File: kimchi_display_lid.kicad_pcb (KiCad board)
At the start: 4 copper layers, 123 x 91 mm, 44 parts, among them J1 DF40HC(3.5)-60DS, J2 DF40HC(3.5)-60DS, J3 H19C-6S-0.5SH, J4 FH19C-40S-0.5SH(10), J5 USB_A, U1 24C32, U2 AP3019AKTR-G1, U3 TXS0108EPW, U4 LSM6DSRTR, U5 TPD3S014

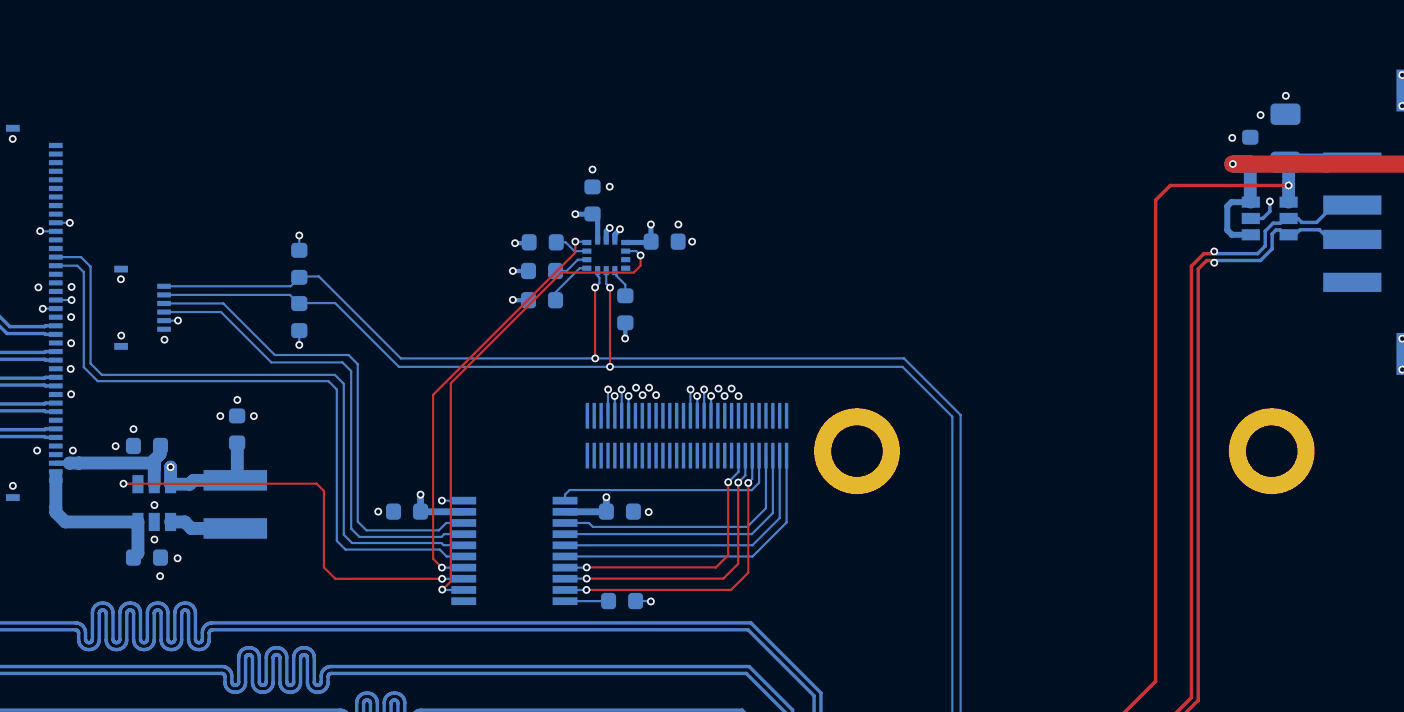
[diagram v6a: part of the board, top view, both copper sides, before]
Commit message: Add a small board to connect touchscreen
When the cables wrap around the PCB the distance between
the 40pin and 6pin connectors is too close.

The "hoverboard" floats over the 40pin connector to
air jordan the 6pin down to the main board via a stacked
connector pair.

Signed-off-by: Michael Welling <mwelling@ieee.org>
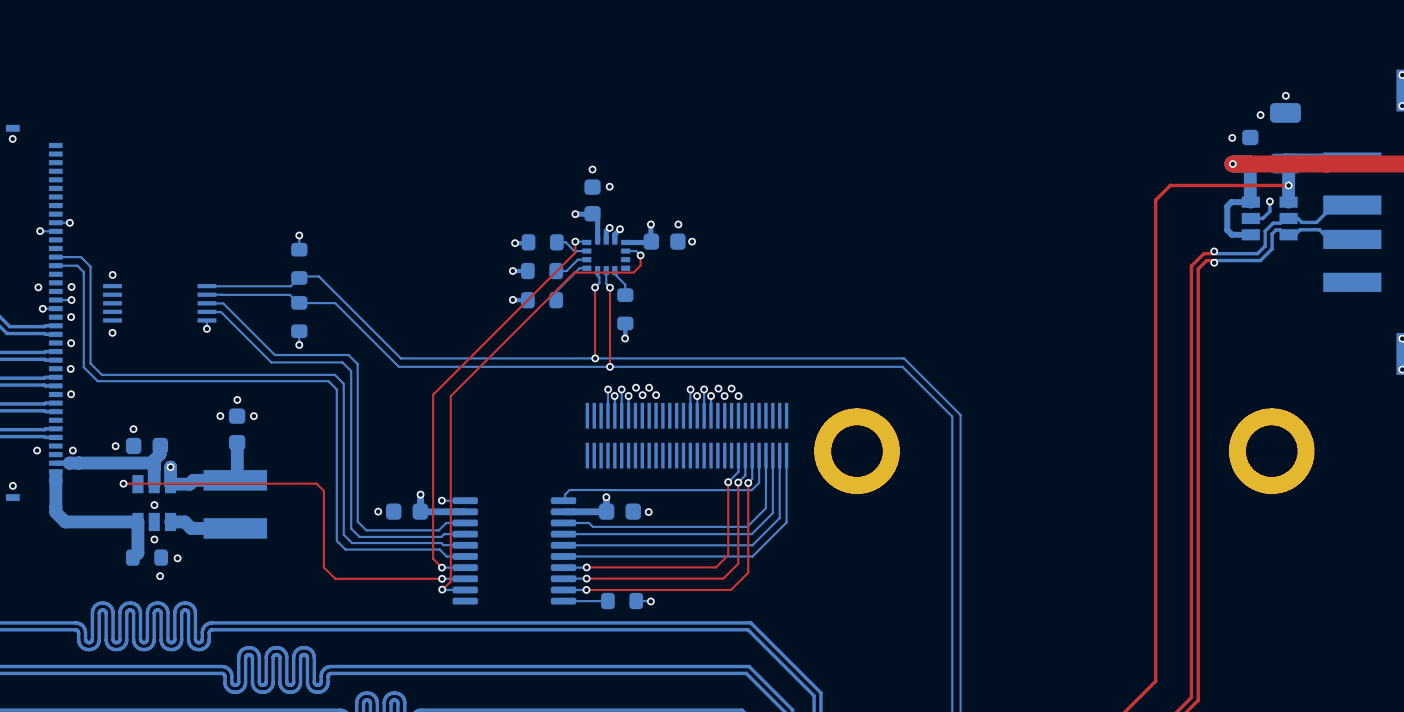
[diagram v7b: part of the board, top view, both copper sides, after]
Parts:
- added LOGO3: Logo_Open_Hardware_Small, kimchi_ulid:hoverboard-3d-model, B.Cu at (116.2, 107.2)
- J3: value H19C-6S-0.5SH -> Conn_02x05_Odd_Even; footprint kimchi_ulid:HRS_FH19C-6S-0.5SH_1x06-1MP_P0.50mm -> kimchi_ulid:HIROSE_DF23C-10DS-0.5V(51)
- moved J3 1.03 mm to (118.0, 107.2), turned to 270 degrees
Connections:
- J3 pad 1: GND -> I2C3_SDA
- J3 pad 2: VDD_3V3 -> GND
- J3 pad 3: /TS_INT -> I2C3_SCL
- J3 pad 4: /TS_RESET -> GND
- J3 pad 5: I2C3_SCL -> /TS_RESET
- J3 pad 6: I2C3_SDA -> GND
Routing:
- net /TS_RESET: track 28.5 -> 26.0 mm
- net /TS_INT: track 28.3 -> 25.8 mm
- net I2C3_SDA: track 102.6 -> 100.1 mm
- net I2C3_SCL: track 100.1 -> 97.6 mm
- net GND: vias 58 -> 57

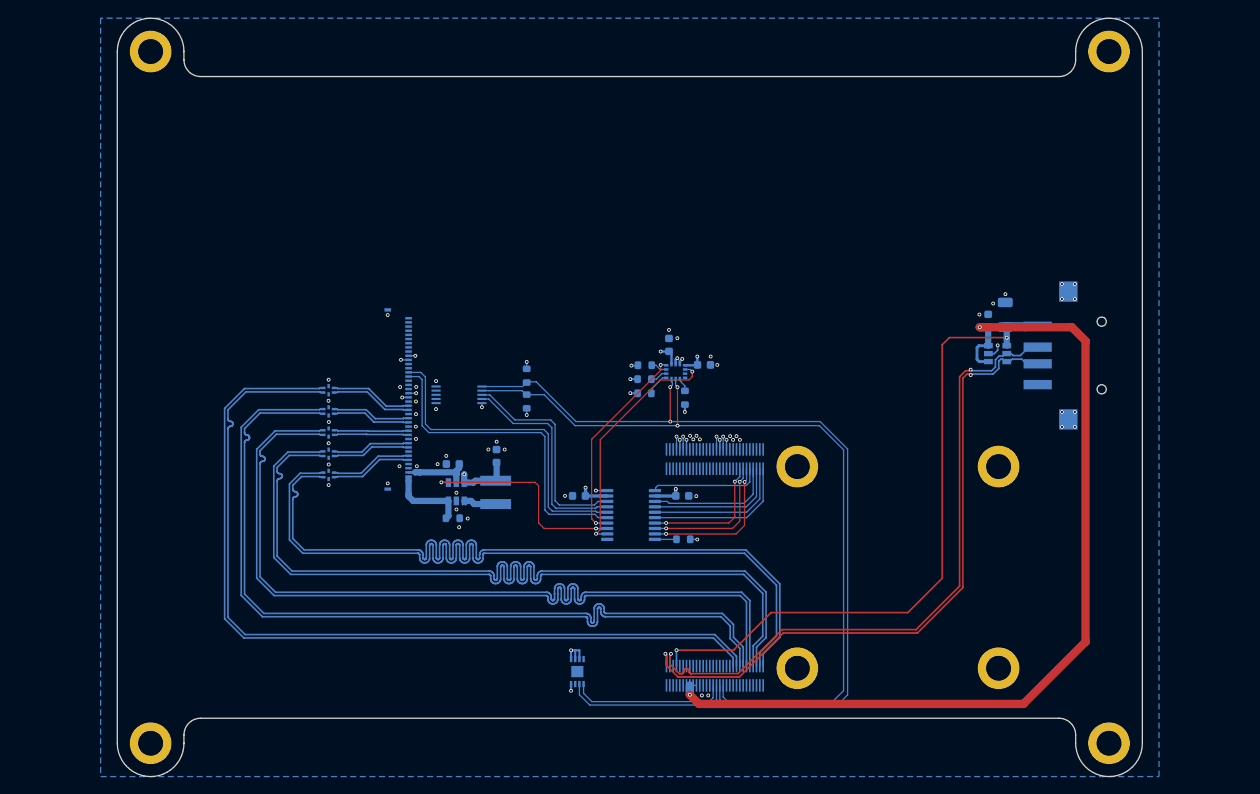
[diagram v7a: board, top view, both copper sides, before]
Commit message: Totally messed up the connections to the hoverboard
Great scott!!

Only caught this after placing an order at OSHpark.
Swiftly cancelled for this fix.

Signed-off-by: Michael Welling <mwelling@ieee.org>
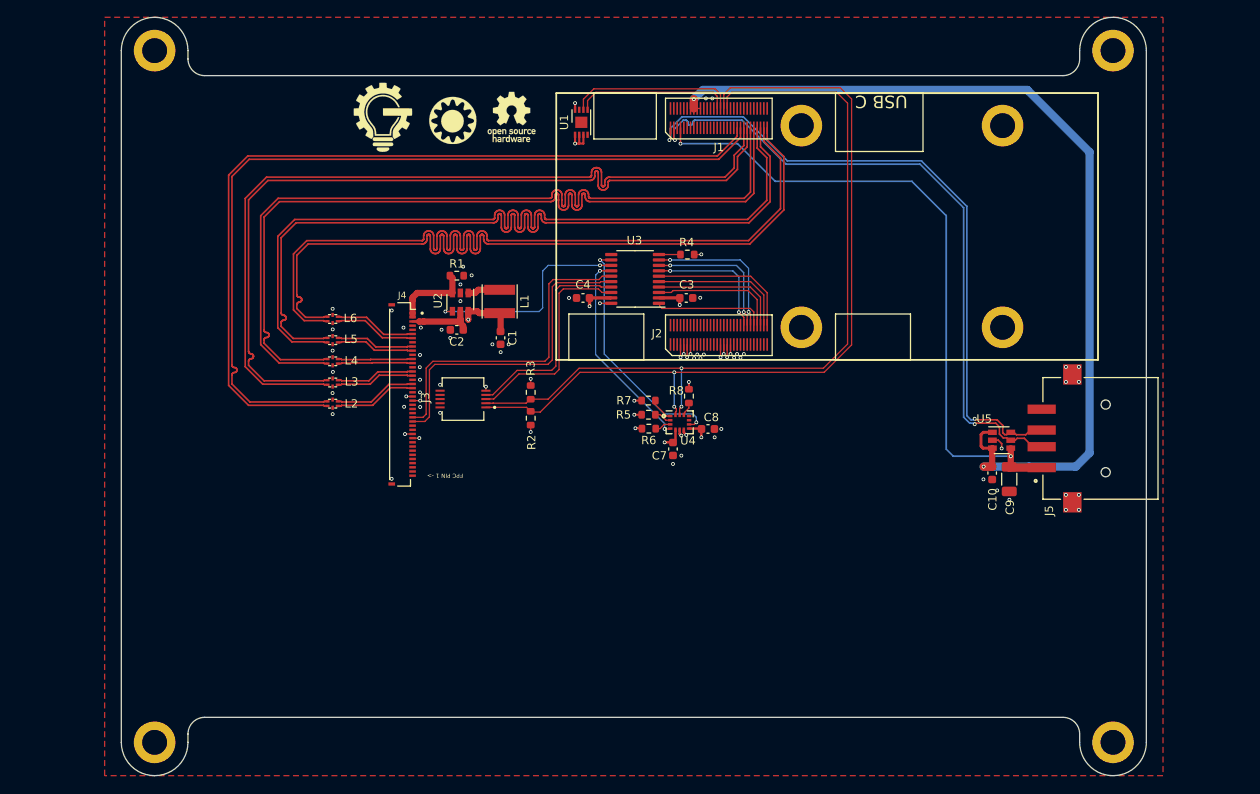
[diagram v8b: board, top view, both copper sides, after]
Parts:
- C1, C10, C2, C3, C4, C7, C8, C9, J1, J2, J3, J4, J5, L1, L2, L3, L4, L5, L6, L7, L8, LOGO1, LOGO2, LOGO3, R1, R2, R3, R4, R5, R6, R7, R8, U1, U2, U3, U4, U5: moved to F.Cu
- H1, H2, H3, H4, H5, H6, H7, H8: moved to B.Cu
- moved H5 83.1 mm to (81.5, 65.9)
- moved H8 83.1 mm to (196.5, 65.9)
- moved H6 82.9 mm to (81.5, 148.9)
- moved H7 82.9 mm to (196.5, 148.9)
- moved LOGO1 67.2 mm to (124.3, 73.8), turned to 0 degrees
- moved L7 67.1 mm to (108.9, 73.9), turned to 0 degrees
- moved J1 66.9 mm to (149.2, 74.0)
- moved L8 66.3 mm to (117.3, 74.3), turned to 180 degrees
- moved U1 65.9 mm to (132.7, 74.5), turned to 90 degrees
- moved H1 65.1 mm to (183.2, 74.9)
- moved H3 65.1 mm to (159.1, 74.9)
- moved LOGO2 40.9 mm to (162.2, 87.0)
- moved R4 34.2 mm to (145.4, 90.4)
- moved R1 29.1 mm to (117.7, 92.9)
- moved U3 28.3 mm to (139.1, 93.3)
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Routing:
- added copper zone on F.Cu, net GND
- added copper zone on In2.Cu, net GND
- added copper zone on In1.Cu, net VDD_1V8
- added copper zone on In1.Cu, net VDD_3V3
- removed copper zone on B.Cu, net GND
- removed copper zone on In1.Cu, net GND
- removed copper zone on In2.Cu, net VDD_1V8
- removed copper zone on In2.Cu, net VDD_3V3
